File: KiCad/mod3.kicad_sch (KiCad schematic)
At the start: 49 parts, among them M5 Fan_4pin, M6 Fan_4pin, U3 ZD25Q64BSIGT

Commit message: Copy modules 2 and 3, remove unnecessary pages
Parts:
- removed D10: B0520W, Diode_SMD:D_SOD-123, symbol Device:D_Schottky
- removed D11, D12: LED, LED_SMD:LED_0603_1608Metric, symbol Device:LED
- removed U3: ZD25Q64BSIGT, Package_SO:SOIC-8_5.3x5.3mm_P1.27mm, symbol Memory_Flash:W25Q128JVS
- added C380, C381, C383, C384, C386, C389: 2.2uF, Capacitor_SMD:C_0402_1005Metric, symbol Device:C_Small
- added C382, C391, C392, C393, C394: 220nF, Capacitor_SMD:C_0402_1005Metric, symbol Device:C_Small
- added C385, C387: 100nF, Capacitor_SMD:C_0402_1005Metric, symbol Device:C_Small
- added C388: 1uF, Capacitor_SMD:C_0402_1005Metric, symbol Device:C_Small
- added C390: 10uF, Capacitor_SMD:C_0402_1005Metric, symbol Device:C_Small
- added C395, C399, C400, C403: 100nF/50V, Capacitor_SMD:C_0402_1005Metric, symbol Device:C
- added C396: 10uF/10V, Capacitor_SMD:C_0603_1608Metric, symbol Device:C
- added C397, C405: 27pF, Capacitor_SMD:C_0402_1005Metric, symbol Device:C_Small
- added C398: 390pF, Capacitor_SMD:C_0402_1005Metric, symbol Device:C
- added C401, C402: 100uF/25V, Capacitor_SMD:CP_Elec_6.3x7.7, symbol Device:C_Polarized
- added C404: 560uF/25V, Capacitor_SMD:CP_Elec_6.3x7.7, symbol Device:C_Polarized
- added C406: 100pF, Capacitor_SMD:C_0402_1005Metric, symbol Device:C_Small
- added D10: LED, LED_SMD:LED_0603_1608Metric, symbol Device:LED
- added D11, D8: B0520W, Diode_SMD:D_SOD-123, symbol Device:D_Schottky
- added J30: RJE361882415, RJE361882145:AMPHENOL_RJE361882415, symbol Custom:1xRJ45+2xUSB3
- added J31: SFF-8654-8i, EasyEDA2KiCAD:CONN-SMD_HBH2-74AT-1-UHR, symbol Custom:SFF-8654-8i
- added J32: Bus_PCI_Express_x4, EasyEDA2KiCAD:PCIE-TH_AAA-PCI-161-K03, symbol Connector:Bus_PCI_Express_x4
- added Q9: 2N7002, Package_TO_SOT_SMD:SOT-23, symbol Transistor_FET:Q_NMOS_GSD
- added R253: 15k, Resistor_SMD:R_0402_1005Metric, symbol Device:R_Small
- added R254, R255, R256, R257: 75R, Resistor_SMD:R_0402_1005Metric, symbol Device:R_Small
- added R258, R259, R40: 4.7k, Resistor_SMD:R_0402_1005Metric, symbol Device:R_Small
- added R260: 2.49k, Resistor_SMD:R_0402_1005Metric, symbol Device:R_Small
- added R261, R263: 100k, Resistor_SMD:R_0402_1005Metric, symbol Device:R_Small
- added R262: 10k, Resistor_SMD:R_0402_1005Metric, symbol Device:R_Small
- added R41: 1k, Resistor_SMD:R_0805_2012Metric, symbol Device:R_Small
- added TR8: QG2439S, Custom:QG2439S, symbol Transformer:30F-51NL
- added U3, U61, U62, U63, U64, U65, U67, U68: H5VU25U, Package_DFN_QFN:Diodes_UDFN-10_1.0x2.5mm_P0.5mm, symbol Power_Protection:D3V3XA4B10LP
- added U66: RTL8125BG-CG, Package_DFN_QFN:QFN-48-1EP_6x6mm_P0.4mm_EP4.2x4.2mm, symbol Custom:RTL8125BG-CG
- added Y9: 25MHz, Crystal:Crystal_SMD_3225-4Pin_3.2x2.5mm, symbol Device:Crystal_GND24
- C69, C70, C71, C72: value 10nF -> 220nF
- C73: value 10nF -> 1uF
- C74: value 10nF -> 2.2uF
- C75, C76: value 10nF -> 10uF
- C77: value 220nF -> 2.2uF
- C78: value 220nF -> 10uF
- C79: value 100nF -> 220nF
- R45: value 4.7k -> 22k
- R46: value 4.7k -> 100R
- R47: value 22k -> 4.7k
- R50: value 100R -> 22k
- R51: value 22k -> 10k
- R52: value 1k -> 2.2k; footprint Resistor_SMD:R_0805_2012Metric -> Resistor_SMD:R_0402_1005Metric
- R53: value 2.2k -> 510R
- R54, R55: value 10k -> 100R
- R56: value 2.2k -> 100R
- R57: value 100k -> 100R
- R58: value 10k -> 510R
- R59: value 10k -> 1k
- R60: value 100k -> 4.7k
- R61: value 10k -> 4.7k
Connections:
- net ETH.Tx0+ is gone; now on net GND: C77.1
- net RUSB.SS_Tx1- is gone; now on net +12V: C60.1
- net SATA2.Rx+ is gone; now on net GND: C75.1
- net SATA2.Rx- is gone; now on net +0V95: C76.1
- net SATA2.Tx+ is gone; now on net GND: C73.1
- net SATA2.Tx- is gone; now on net +0V95: C74.1
- net UART_RX is gone; now on an unnamed net: A3.137 (UART0_RXD)
- net UART_TX is gone; now on an unnamed net: A3.139 (UART0_TXD)
- net +12V: now also D9.1 (K), R47.1, C399.1, C400.1, C401.1, C402.1, J32.A2 (+12V), J32.A3 (+12V), J32.B1 (+12V), J32.B2 (+12V), J32.B3 (+12V); no longer C58.1, R46.1
- net +3V3: now also R52.1, R60.1, C403.1, C404.1, J32.A10 (+3.3V), J32.A9 (+3.3V), J32.B8 (+3.3V), R262.2; no longer C79.1, R53.1, R56.2, R58.1
- net +5V: now also D8.1 (K), J30.U1 (VBUS), J30.U10 (VBUS), R40.1; no longer D9.1 (K), R45.1
- net +BATT: now also R41.1; no longer R52.1
- net GND: now also C60.2, C74.2, C76.2, C78.2, R50.2, C380.1, C381.2, C383.1, C384.2, C385.1, C386.2, C387.1, C388.2, C389.1, C390.2, C395.1, C396.1, C397.1, C398.1, C399.2, C400.2, C401.2, C402.2, C403.2, C404.2, C405.1, C406.2, J30.SH, J30.U13 (GND), J30.U16 (DRAIN), J30.U4 (GND), J30.U7 (DRAIN), J31.A1 (GND), J31.A10 (GND), J31.A13 (GND), J31.A16 (GND), J31.A19 (GND), J31.A22 (GND), J31.A25 (GND), J31.A28 (GND), J31.A31 (GND), J31.A34 (GND), J31.A37 (GND), J31.A4 (GND), J31.A7 (GND), J31.B1 (GND), J31.B10 (GND), J31.B12 (CPRSNTA#), J31.B13 (GND), J31.B16 (GND), J31.B19 (GND), J31.B22 (GND), J31.B25 (GND), J31.B28 (GND), J31.B30 (CPRSNTB#), J31.B31 (GND), J31.B34 (GND), J31.B37 (GND), J31.B4 (GND), J31.B7 (GND), J31.SH, J31.SH, J32.A1 (~{PRSNT1}), J32.A12 (GND), J32.A15 (GND), J32.A18 (GND), J32.A20 (GND), J32.A23 (GND), J32.A24 (GND), J32.A27 (GND), J32.A28 (GND), J32.A31 (GND), J32.A4 (GND), J32.B13 (GND), J32.B16 (GND), J32.B17 (~{PRSNT2}), J32.B18 (GND), J32.B21 (GND), J32.B22 (GND), J32.B25 (GND), J32.B26 (GND), J32.B29 (GND), J32.B31 (~{PRSNT2}), J32.B32 (GND), J32.B4 (GND), J32.B7 (GND), Q9.2 (S), R253.2, R260.2, R261.1, R263.1, U3.3 (VSS), U3.8 (VSS), U61.3 (VSS), U61.8 (VSS), U62.3 (VSS), U62.8 (VSS), U63.3 (VSS), U63.8 (VSS), U64.3 (VSS), U64.8 (VSS), U65.3 (VSS), U65.8 (VSS), U66.40 (GND), U66.49 (GND), U67.3 (VSS), U67.8 (VSS), U68.3 (VSS), U68.8 (VSS), Y9.2, Y9.4; no longer C58.2, C79.2, R54.2, R55.2, R57.1, R60.1, R61.2
- net CASE_FAN_PWM: now reaches R49.1
- net CASE_FAN_PWM: now also A3.6 (FAN2_PWM); no longer A3.2 (FAN1_PWM)
- net at R49.2: now also M6.4 (PWM); no longer M5.4 (PWM)
- net at A3.55 (HSIO11_TX+): now also C79.2; no longer C73.2
- net at A3.49 (HSIO10_TX+): now also C71.2; no longer C69.2
- net at R56.1: now also A3.141 (UART1_RXD)
- net at R55.1: no longer A3.102 (~{CLKREQ4})
- net CASE_FAN_TAC: now reaches A3.8 (FAN2_TAC), R48.1
- net CASE_FAN_TAC: now also R50.1; no longer R51.1
- net at M6.3 (Tacho), R48.2: now also D9.2 (A), R47.2; no longer R46.2
- net PCIEX4_RX2+: now reaches A3.52 (HSIO10_RX+)
- net PCIEX4_RX2+: now also J32.A25 (PERp2); no longer C71.2
- net at A3.161 (SPI_IO2): no longer R59.2
- net at R54.1: no longer A3.100 (~{CLKREQ3})
- net at R52.2: now also D10.2 (A); no longer A3.115 (VBAT)
- net at C59.2: now also A3.15 (HSIO0_TX-); no longer A3.13 (HSIO0_TX+)
- net at A3.133 (~{BIOS_SEL}): now also R262.1; no longer R61.1
- net at A3.143 (UART1_TXD): now also R57.1
- net at A3.153 (SPI_IO3): no longer R58.2
- net at A3.183 (DDIB_HPD): now also R62.2; no longer R57.2
- net at A3.185 (TCP1_HPD): now also R263.2; no longer R62.2
- net at A3.187 (TCP0_HPD): now also R261.2; no longer R60.2
- net at A3.31 (HSIO3_TX+): now also C65.2
- net at A3.33 (HSIO3_TX-): now also C66.2
- net NVME1_RX+: now reaches A3.34 (HSIO3_RX+)
- net NVME1_RX+: now also J31.A20 (PERp4)
- net NVME1_RX-: now reaches A3.36 (HSIO3_RX-)
- net NVME1_RX-: now also J31.A21 (PERn4)
- net at A3.37 (HSIO8_TX+): now also C67.2; no longer C65.2
- net at A3.39 (HSIO8_TX-): now also C68.2; no longer C66.2
- net CPU_FAN_TAC: now reaches A3.4 (FAN1_TAC)
- net CPU_FAN_TAC: now also R45.1; no longer R47.1
- net at A3.43 (HSIO9_TX+): now also C69.2; no longer C67.2
- net at A3.45 (HSIO9_TX-): now also C70.2; no longer C68.2
- net POWER_S0: now reaches A3.5 (SLS_S0)
- net POWER_S0: now also R59.2, Q9.1 (G), R253.1, U66.1 (~{ISOLATEB})
- net at A3.51 (HSIO10_TX-): now also C72.2; no longer C70.2
- net PCIEX4_RX2-: now reaches A3.54 (HSIO10_RX-)
- net PCIEX4_RX2-: now also J32.A26 (PERn2); no longer C72.2
- net at A3.57 (HSIO11_TX-): now also C382.2; no longer C74.2
- net +3V3SB: now reaches C75.2
- net +3V3SB: now also C73.2, C77.2, R53.2, R58.2, R61.1, C380.2, C383.2, C385.2, C387.2, C389.2, C395.2, C396.2, J32.B10 (3.3Vaux), R258.2, R259.2, U66.15 (AVDD33), U66.19 (AVDD33), U66.29 (DVDD33), U66.33 (AVDD33), U66.34 (AVDD33_XTAL), U66.43 (EVDD33), U66.46 (DVDD33); no longer A3.58 (HSIO11_RX+)
- net PCIEX4_RX3-: now reaches A3.60 (HSIO11_RX-)
- net PCIEX4_RX3-: now also J32.A30 (PERn3); no longer C76.2
- net at A3.61 (HSIO6_TX+): now also C391.2; no longer C77.2
- net at A3.63 (HSIO6_TX-): now also C392.2; no longer C78.2
- net ETH_REFCLK+: now reaches A3.88 (REFCLK3+)
- net ETH_REFCLK+: now also U66.44 (REFCLK+)
- net ETH_REFCLK-: now reaches A3.90 (REFCLK3-)
- net ETH_REFCLK-: now also U66.45 (REFCLK-)
- net at M5.3 (Tacho), R45.2: now also D8.2 (A), R40.2; no longer D9.2 (A), R47.2
- net ETH.REFCLK+ renamed NVME0_REFCLK+
- net NVME0_REFCLK+: now also J31.A11 (REFCLKA+)
- net ETH.REFCLK- renamed NVME0_REFCLK-
- net NVME0_REFCLK-: now also J31.A12 (REFCLKA-)
- net ETH.Rx0+ renamed ETH_RX+
- net ETH_RX+: now also C393.1
- net ETH.Rx0- renamed ETH_RX-
- net ETH_RX-: now also C394.1
- net ETH.SMBCLK renamed SMB_DATA
- net SMB_DATA: now also J31.B27 (2W-DATAB), J31.B9 (2W-DATAA), J32.B6 (SMDAT)
- net ETH.SMBDAT renamed SMB_CLK
- net SMB_CLK: now also J31.B26 (2W-CLKB), J31.B8 (2W-CLKA), J32.B5 (SMCLK)
- net ETH.Tx0- renamed +0V95
- net +0V95: now also C381.1, C384.1, C386.1, C388.1, C390.1, U66.11 (AVDD09), U66.16 (AVDD09), U66.22 (AVDD09), U66.28 (DVDD09), U66.37 (EVDD09), U66.47 (DVDD09), U66.8 (DVDD09)
- net ETH.~{PLTRST} renamed ~{PCIE_RST}
- net ~{PCIE_RST}: now also J31.B11 (PERSTA#), J31.B29 (PERSTB#), J32.A11 (~{PERST}), U66.36 (~{PERRST})
- net ETH.~{WAKE} renamed ~{PCIE_WAKE}
- net ~{PCIE_WAKE}: now also R61.2, J31.A27 (CWAKEB#), J31.A9 (CWAKEA#), J32.B11 (~{WAKE}), U66.2 (LANWAKEB)
- net FUSB.D+ renamed RUSB1_D+
- net RUSB1_D+: now also J30.U11 (D-), U3.4, U3.7 (NC)
- net FUSB.D- renamed RUSB1_D-
- net RUSB1_D-: now also J30.U12 (D+), U3.5, U3.6 (NC)
- net FUSB.SS_Rx1+ renamed RUSB1_SSRX+
- net RUSB1_SSRX+: now also J30.U14 (SSRX-), U62.1, U62.10 (NC)
- net FUSB.SS_Rx1- renamed RUSB1_SSRX-
- net RUSB1_SSRX-: now also J30.U15 (SSRX+), U62.2, U62.9 (NC)
- net FUSB.SS_Tx1+ renamed RUSB1_SSTX+
- net RUSB1_SSTX+: now also J30.U17 (SSTX-), U62.4, U62.7 (NC)
- net FUSB.SS_Tx1- renamed RUSB1_SSTX-
- net RUSB1_SSTX-: now also J30.U18 (SSTX+), U62.5, U62.6 (NC)
- net M2_EKEY.REFCLK+ renamed PCIEX4_REFCLK+
- net PCIEX4_REFCLK+: now also J32.A13 (REFCLK+)
- net M2_EKEY.REFCLK- renamed PCIEX4_REFCLK-
- net PCIEX4_REFCLK-: now also J32.A14 (REFCLK-)
- net M2_EKEY.Rx0+ renamed NVME0_RX+
- net NVME0_RX+: now also J31.A2 (PERp0)
- net M2_EKEY.Rx0- renamed NVME0_RX-
- net NVME0_RX-: now also J31.A3 (PERn0)
- net M2_EKEY.SUSCLK: no longer names the net of A3.131 (SUSCLK)
- net M2_EKEY.Tx0+ renamed NVME0_TX+
- net NVME0_TX+: now also J31.B2 (PETp0)
- net M2_EKEY.Tx0- renamed NVME0_TX-
- net NVME0_TX-: now also J31.B3 (PETn0)
- net M2_EKEY.USB-D+: no longer names the net of A3.81 (USB2_P3+)
- net M2_EKEY.USB-D-: no longer names the net of A3.79 (USB2_P3-)
- net NVME.REFCLK+ renamed NVME1_REFCLK+
- net NVME1_REFCLK+: now also J31.A29 (REFCLKB+)
- net NVME.REFCLK- renamed NVME1_REFCLK-
- net NVME1_REFCLK-: now also J31.A30 (REFCLKB-)
- net NVME.Rx0+ renamed PCIEX4_RX0+
- net PCIEX4_RX0+: now also J32.A16 (PERp0)
- net NVME.Rx0- renamed PCIEX4_RX0-
- net PCIEX4_RX0-: now also J32.A17 (PERn0)
- net NVME.Rx1+ renamed PCIEX4_RX1+
- net PCIEX4_RX1+: now also J32.A21 (PERp1)
- net NVME.Rx1- renamed PCIEX4_RX1-
- net PCIEX4_RX1-: now also J32.A22 (PERn1)
- net NVME.Tx0+ renamed NVME1_TX+
- net NVME1_TX+: now also J31.B20 (PETp4)
- net NVME.Tx0- renamed NVME1_TX-
- net NVME1_TX-: now also J31.B21 (PETn4)
- net NVME.Tx1+ renamed PCIEX4_TX0+
- net PCIEX4_TX0+: now also J32.B14 (PETp0)
- net NVME.Tx1- renamed PCIEX4_TX0-
- net PCIEX4_TX0-: now also J32.B15 (PETn0)
- net RUSB.D+ renamed RUSB0_D+
- net RUSB0_D+: now also J30.U2 (D-), U3.1, U3.10 (NC)
- net RUSB.D- renamed RUSB0_D-
- net RUSB0_D-: now also J30.U3 (D+), U3.2, U3.9 (NC)
- net RUSB.SS_Rx1+ renamed RUSB0_SSRX+
- net RUSB0_SSRX+: now also J30.U5 (SSRX-), U61.1, U61.10 (NC)
- net RUSB.SS_Rx1- renamed RUSB0_SSRX-
- net RUSB0_SSRX-: now also J30.U6 (SSRX+), U61.2, U61.9 (NC)
- net RUSB.SS_Tx1+ renamed RUSB0_SSTX-
- net RUSB0_SSTX-: now also J30.U9 (SSTX+), U61.5, U61.6 (NC)
- net SATA1.Rx+ renamed PCIEX4_TX2+
- net PCIEX4_TX2+: now also J32.B23 (PETp2)
- net SATA1.Rx- renamed PCIEX4_TX2-
- net PCIEX4_TX2-: now also J32.B24 (PETn2)
- net SATA1.Tx+ renamed PCIEX4_TX1+
- net PCIEX4_TX1+: now also J32.B19 (PETp1)
- net SATA1.Tx- renamed PCIEX4_TX1-
- net PCIEX4_TX1-: now also J32.B20 (PETn1)
- new net: C397.2, U66.10 (CKXTAL1), Y9.1
- new net: R256.1, TR8.18 (CT)
- new net: C406.1, R254.2, R255.2, R256.2, R257.2
- new net: R254.1, TR8.24 (CT)
- new net: J30.1, TR8.13 (MX4-)
- new net: J30.2, TR8.14 (MX4+)
- new net: R257.1, TR8.15 (CT)
- new net: J30.3, TR8.16 (MX3-)
- new net: J30.6, TR8.17 (MX3+)
- new net: J30.4, TR8.19 (MX2-)
- new net: J30.5, TR8.20 (MX2+)
- new net: R255.1, TR8.21 (CT)
- new net: J30.7, TR8.22 (MX1-)
- new net: J30.8, TR8.23 (MX1+)
- new net: C393.2, U66.38 (Tx+)
- new net: J30.D1, R58.1
- new net: J30.D3, R53.1
- new net: M5.4 (PWM), R46.2
- new net: D10.1 (K), Q9.3 (D)
- new net: C405.2, U66.9 (CKXTAL2), Y9.3
- new net: D11.2 (A), U66.6 (POW_EXT_SWR)
- new net: A3.102 (~{CLKREQ4}), R51.1
- new net: R260.1, U66.12 (RSET)
- new net: A3.115 (VBAT), R41.2
- new net: A3.13 (HSIO0_TX+), C58.2
- new net: R258.1, U66.3 (GPI)
- new net: C394.2, U66.39 (Tx-)
- new net: U66.4 (NC), U66.5 (NC), U66.7 (NC)
- new net 0V95_ENABLE: D11.1 (K)
- new net BMC_UART_RX: R54.2
- new net BMC_UART_TX: R55.2
- new net CPU_FAN_PWM: A3.2 (FAN1_PWM), R46.1
- new net ETH_LED0: J30.D4, U66.30 (EEDI/SDA)
- new net ETH_LED1: J30.D2, R259.1, U66.27 (EESK)
- new net ETH_TX+: C391.1, U66.41 (Rx+)
- new net ETH_TX-: C392.1, U66.42 (Rx-)
- new net HDMI_CK+: U67.4, U67.7 (NC)
- new net HDMI_CK-: U67.5, U67.6 (NC)
- new net HDMI_D0+: U67.1, U67.10 (NC)
- new net HDMI_D0-: U67.2, U67.9 (NC)
- new net HDMI_D1+: U65.4, U65.7 (NC)
- new net HDMI_D1-: U65.5, U65.6 (NC)
- new net HDMI_D2+: U65.1, U65.10 (NC)
- new net HDMI_D2-: U65.2, U65.9 (NC)
- new net HDMI_HPDO: U68.5, U68.6 (NC)
- new net HDMI_SCLO: U68.1, U68.10 (NC)
- new net HDMI_SDAO: U68.2, U68.9 (NC)
- new net MDI0+: TR8.12 (TD4-), U63.1, U63.10 (NC), U66.13 (MDI[0]+)
- new net MDI0-: TR8.11 (TD4+), U63.2, U63.9 (NC), U66.14 (MDI[0]-)
- new net MDI1+: TR8.9 (TD3-), U63.4, U63.7 (NC), U66.17 (MDI[1]+)
- new net MDI1-: TR8.8 (TD3+), U63.5, U63.6 (NC), U66.18 (MDI[1]-)
- new net MDI2+: TR8.6 (TD2-), U64.1, U64.10 (NC), U66.20 (MDI[2]+)
- new net MDI2-: TR8.5 (TD2+), U64.2, U64.9 (NC), U66.21 (MDI[2]-)
- new net MDI3+: TR8.3 (TD1-), U64.4, U64.7 (NC), U66.23 (MDI[3]+)
- new net MDI3-: C398.2, TR8.1 (CT), TR8.10 (CT), TR8.2 (TD1+), TR8.4 (CT), TR8.7 (CT), U64.5, U64.6 (NC), U66.24 (MDI[3]-)
- new net PCIEX4_RX3+: A3.58 (HSIO11_RX+), J32.A29 (PERp3)
- new net PCIEX4_TX3+: C79.1, J32.B27 (PETp3)
- new net PCIEX4_TX3-: C382.1, J32.B28 (PETn3)
- new net RUSB0_SSTX+: C58.1, J30.U8 (SSTX-), U61.4, U61.7 (NC)
- new net SLOT1_UART_RX: R56.2
- new net SLOT1_UART_TX: R57.2
- new net ~{ETH_CLKREQ}: A3.100 (~{CLKREQ3}), R60.2, U66.48 (CLKREQB)
- no-connect marks 111 -> 154
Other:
- note added: "2.5G Ethernet"
- note added: "2x U.2 NVME"
- note added: "Fans"
- note added: "LattePanda Mu Module"
- note added: "PCIe x4 Slot"
- note added: "Power LED"
- note added: "USB 3"

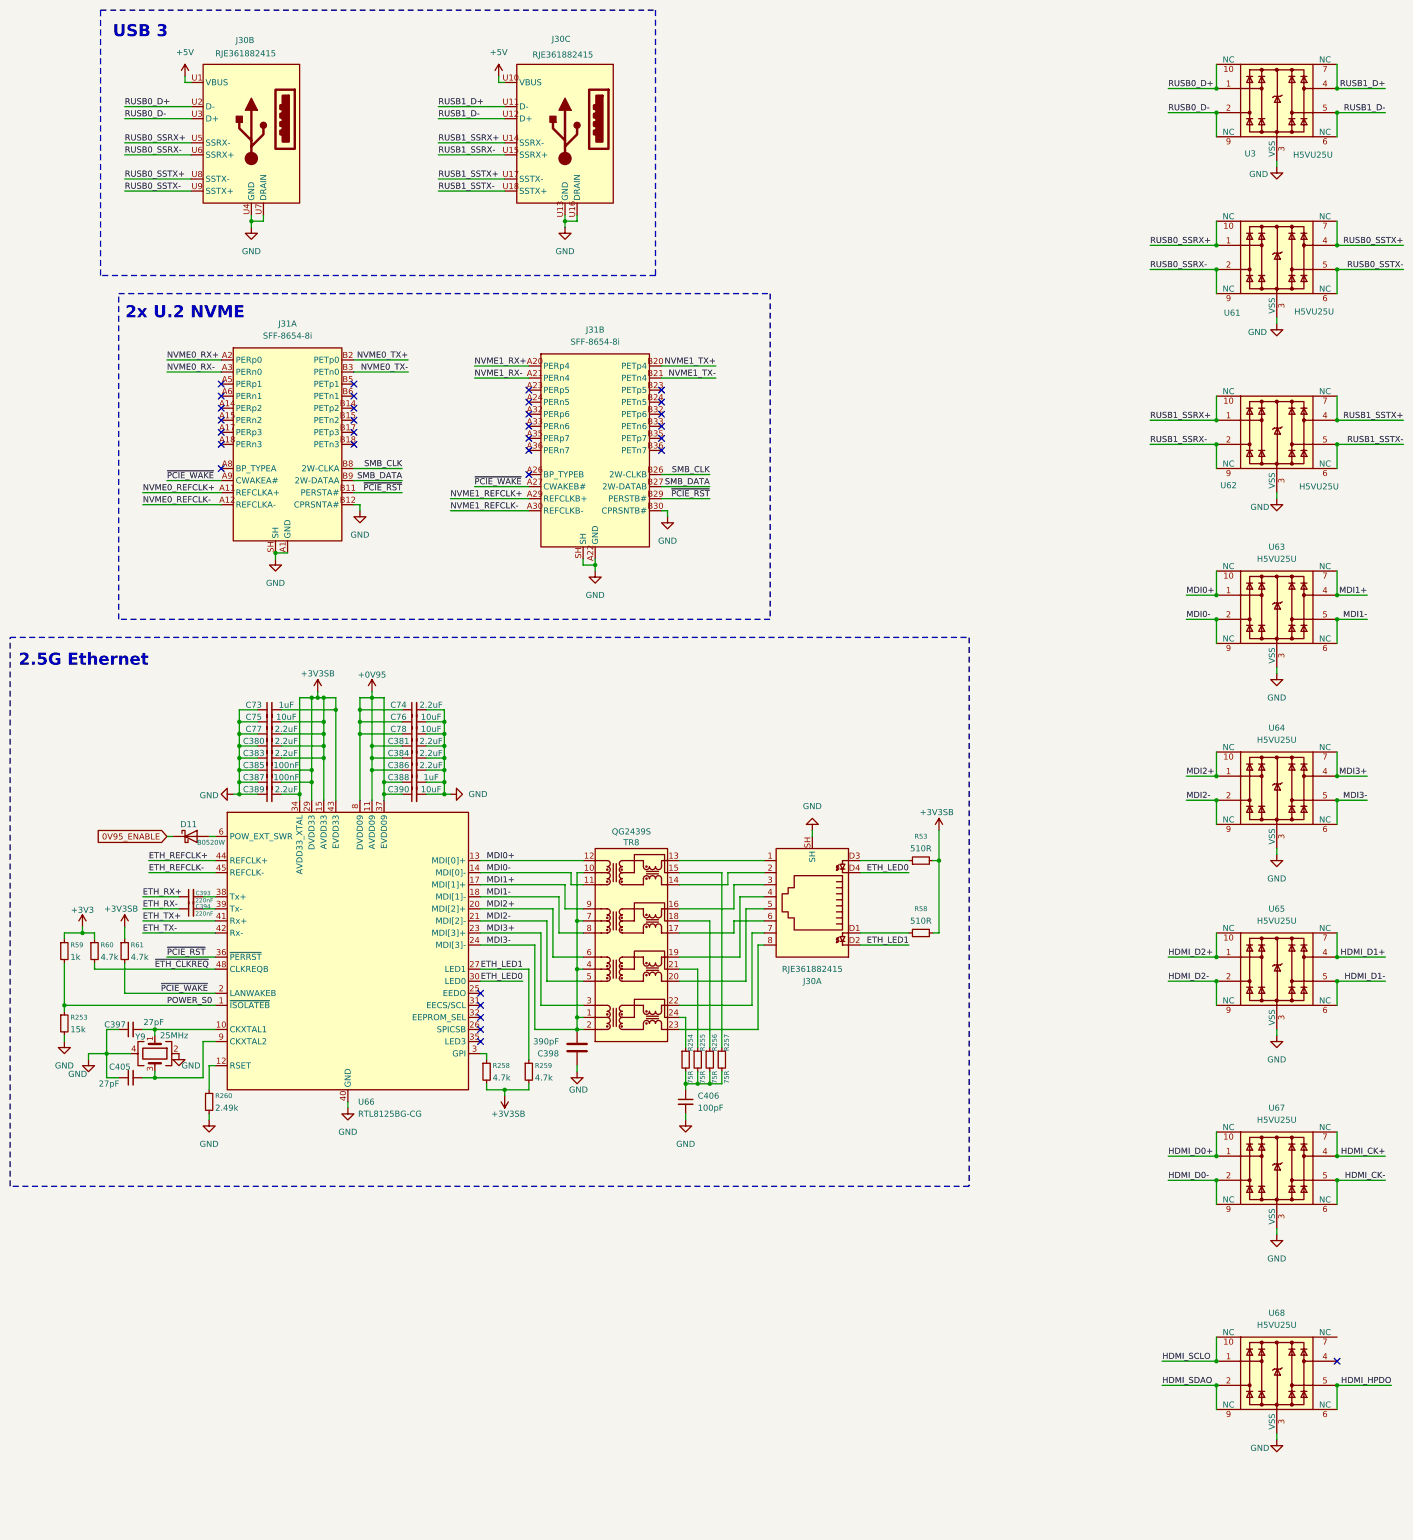
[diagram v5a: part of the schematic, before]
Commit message: Add 0.95V supply, Fix connectors
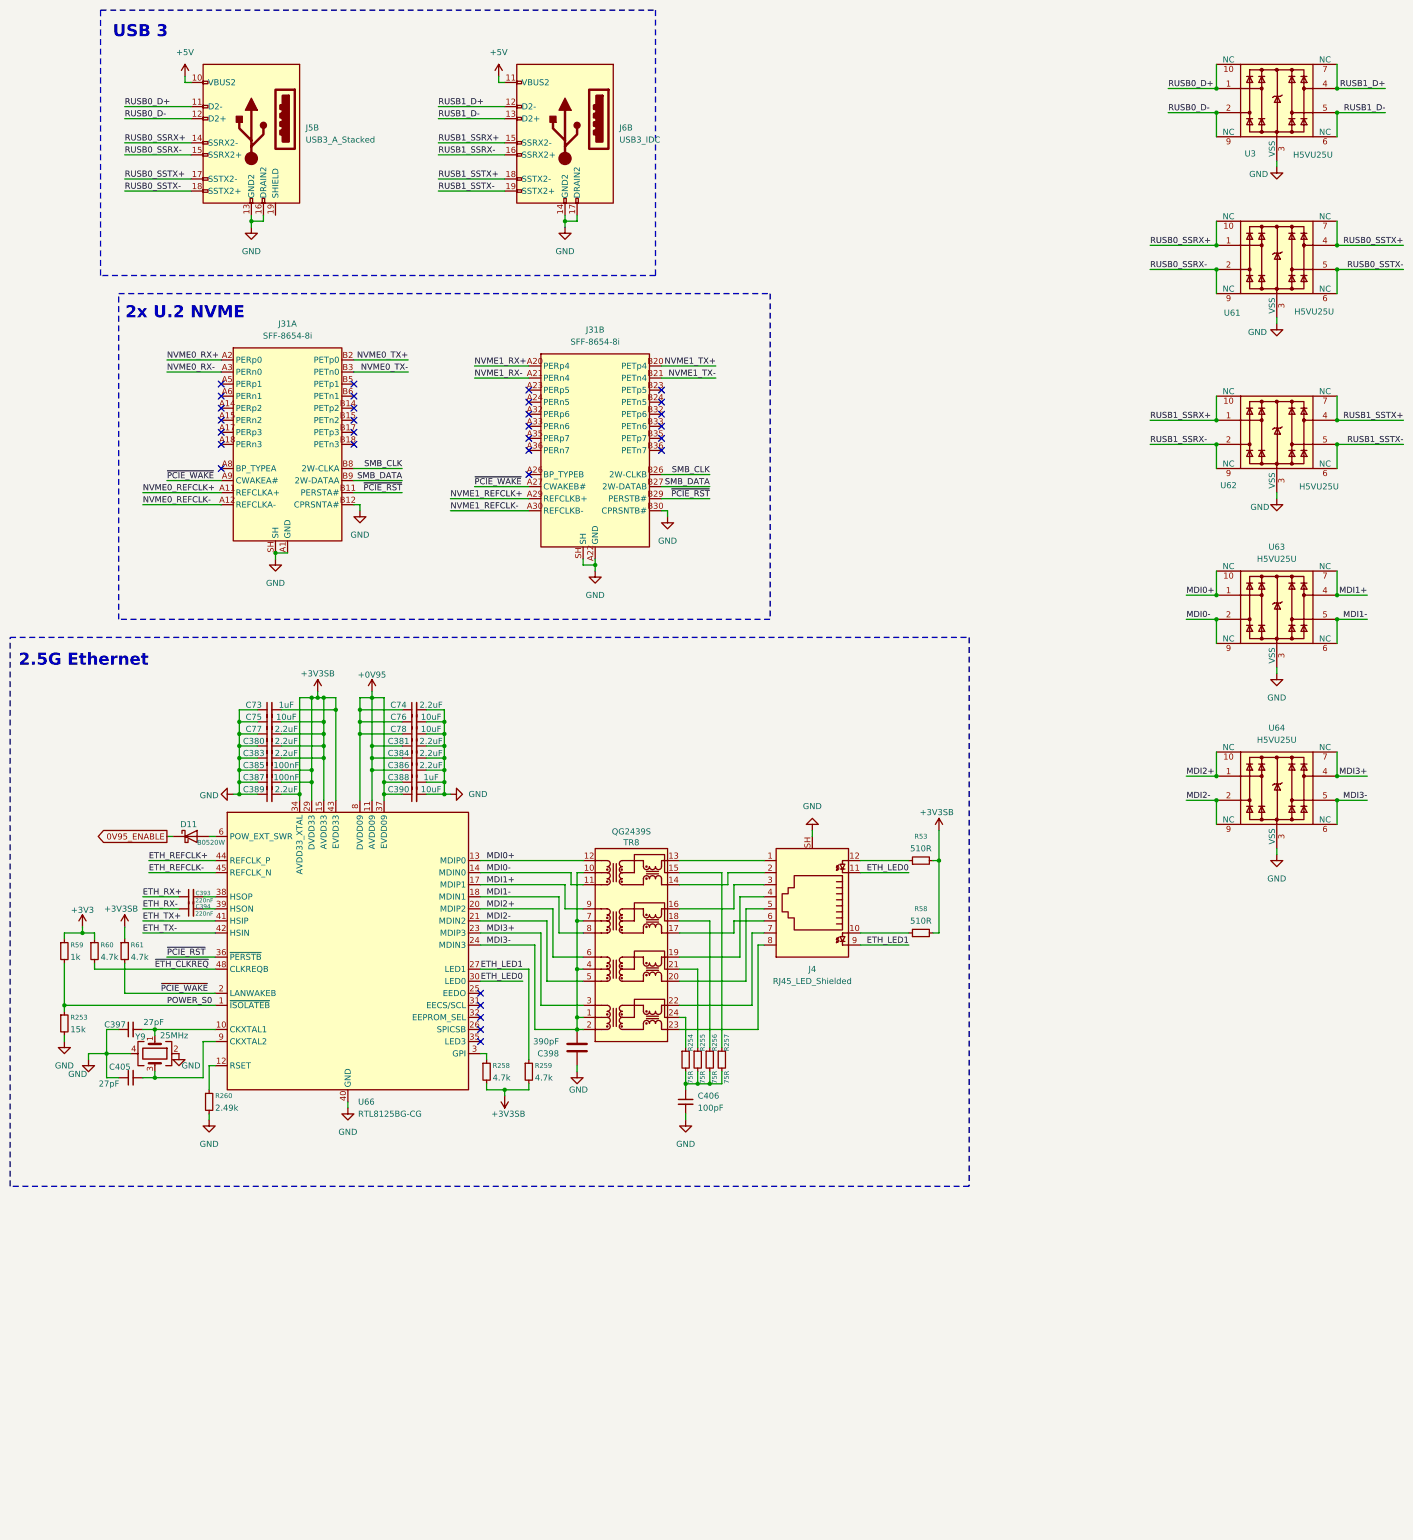
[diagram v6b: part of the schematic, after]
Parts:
- removed J30: RJE361882415, RJE361882145:AMPHENOL_RJE361882415, symbol Custom:1xRJ45+2xUSB3
- removed U65, U67, U68: H5VU25U, Package_DFN_QFN:Diodes_UDFN-10_1.0x2.5mm_P0.5mm, symbol Power_Protection:D3V3XA4B10LP
- added J4: RJ45_LED_Shielded, Connector_RJ:RJ45_Amphenol_RJHSE538X, symbol Connector:RJ45_LED_Shielded
- added J5: USB3_A_Stacked, EasyEDA2KiCAD:USB-A-TH_HC-USB3.0-L175-2X1-J, symbol Connector:USB3_A_Stacked
- added J6: USB3_IDC, Connector_IDC:IDC-Header_2x10_P2.54mm_Vertical, symbol Custom:USB3_IDC
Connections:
- net +5V: now also J5.10 (VBUS2), J6.11 (VBUS2)
- net ETH_LED0: now also J4.11
- net ETH_LED1: now also J4.9
- net GND: now also J4.SH, J5.13 (GND2), J5.16 (DRAIN2), J6.14 (GND2), J6.17 (DRAIN2)
- net RUSB0_D+: now also J5.11 (D2-)
- net RUSB0_D-: now also J5.12 (D2+)
- net RUSB0_SSRX+: now also J5.14 (SSRX2-)
- net RUSB0_SSRX-: now also J5.15 (SSRX2+)
- net RUSB0_SSTX+: now also J5.17 (SSTX2-)
- net RUSB0_SSTX-: now also J5.18 (SSTX2+)
- net RUSB1_D+: now also J6.12 (D2-)
- net RUSB1_D-: now also J6.13 (D2+)
- net RUSB1_SSRX+: now also J6.15 (SSRX2-)
- net RUSB1_SSRX-: now also J6.16 (SSRX2+)
- net RUSB1_SSTX+: now also J6.18 (SSTX2-)
- net RUSB1_SSTX-: now also J6.19 (SSTX2+)
- net at TR8.13 (MX4-): now also J4.1
- net at TR8.14 (MX4+): now also J4.2
- net at TR8.16 (MX3-): now also J4.3
- net at TR8.17 (MX3+): now also J4.6
- net at TR8.19 (MX2-): now also J4.4
- net at TR8.20 (MX2+): now also J4.5
- net at TR8.22 (MX1-): now also J4.7
- net at TR8.23 (MX1+): now also J4.8
- net at R58.1: now also J4.10
- net at R53.1: now also J4.12
- no-connect marks 154 -> 153
